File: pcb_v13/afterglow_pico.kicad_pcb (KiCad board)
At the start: 4 copper layers, 70.1 x 88.1 mm, 94 parts, among them J1 USB_B_Micro, J4 Conn_02x17_Odd_Even, J5 Conn_02x17_Odd_Even, SW1 SW_Push, U1 NCP1117-3.3_SOT223, U10 74HC257, U11 74HC257, U2 RP2040, U3 SN74LVC245AN, U4 SN74LVC245AN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

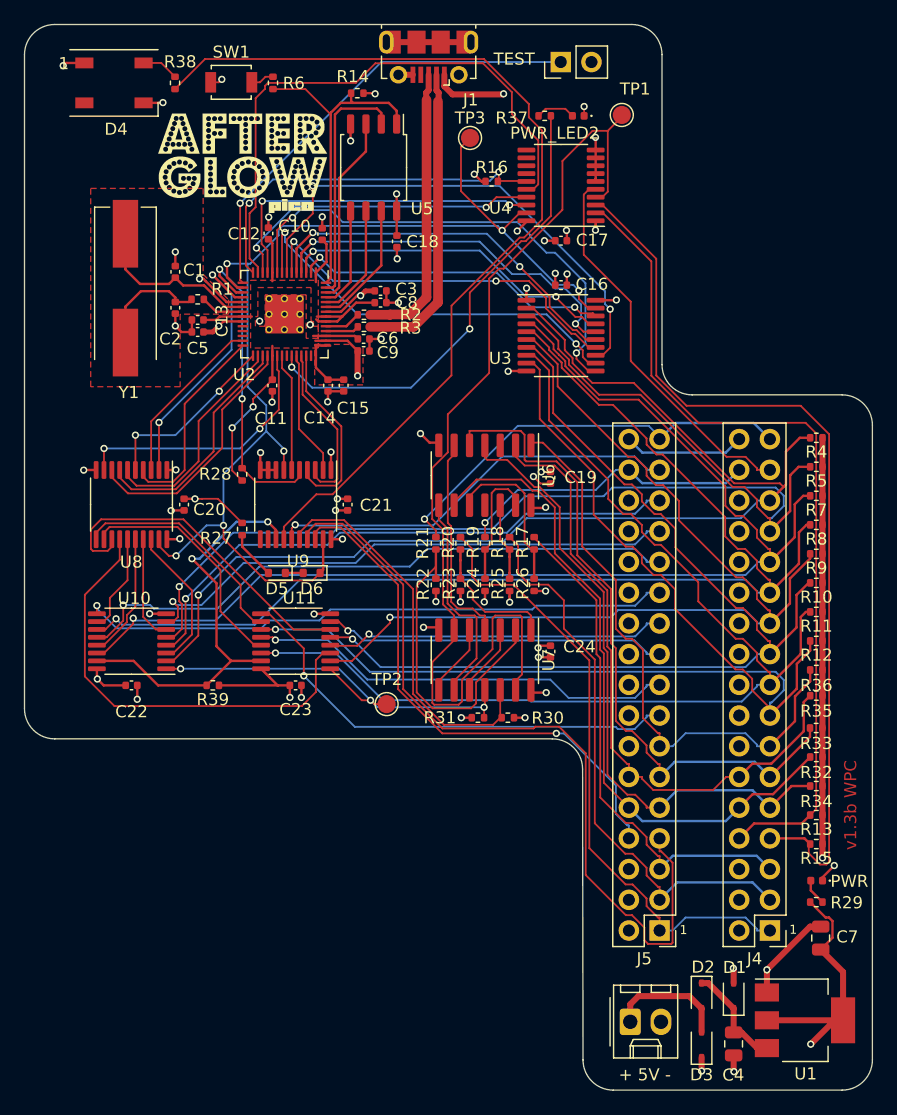
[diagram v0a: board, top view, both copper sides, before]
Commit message: PCB v1.c fixes track cleareance issues
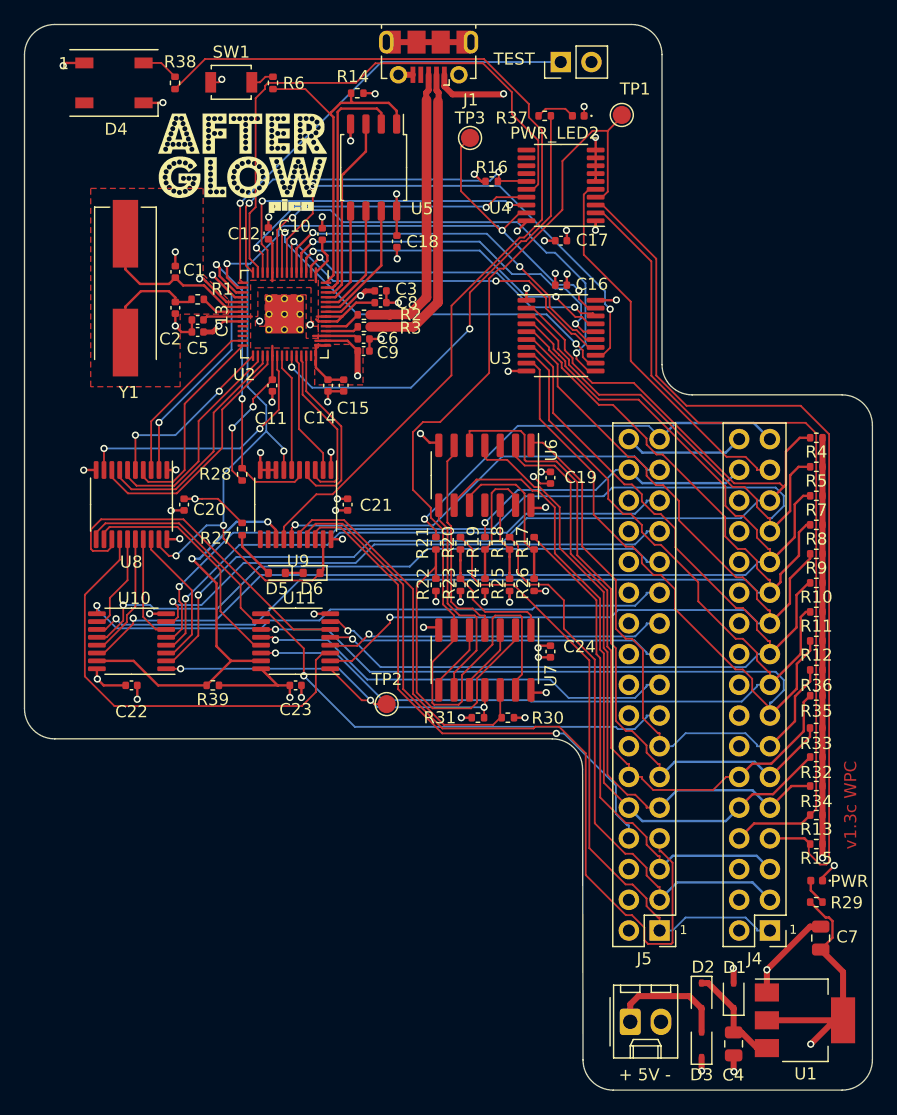
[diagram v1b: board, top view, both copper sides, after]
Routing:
- net /COMB_EV: track 83.4 -> 85.5 mm
- net /GPIO14: track 26.2 -> 27.2 mm
- net Net-(U6-Pad8): track 18.1 -> 18.8 mm
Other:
- board text added: "v1.3c WPC"
- board text removed: "v1.3b WPC"

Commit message: PCB v1.3c
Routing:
- net Net-(R19-Pad1): track 12.0 -> 11.0 mm
- net /SOL3: track 56.0 -> 56.6 mm
